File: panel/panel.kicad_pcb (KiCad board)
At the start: 2 copper layers, 40 x 40 mm, 256 parts

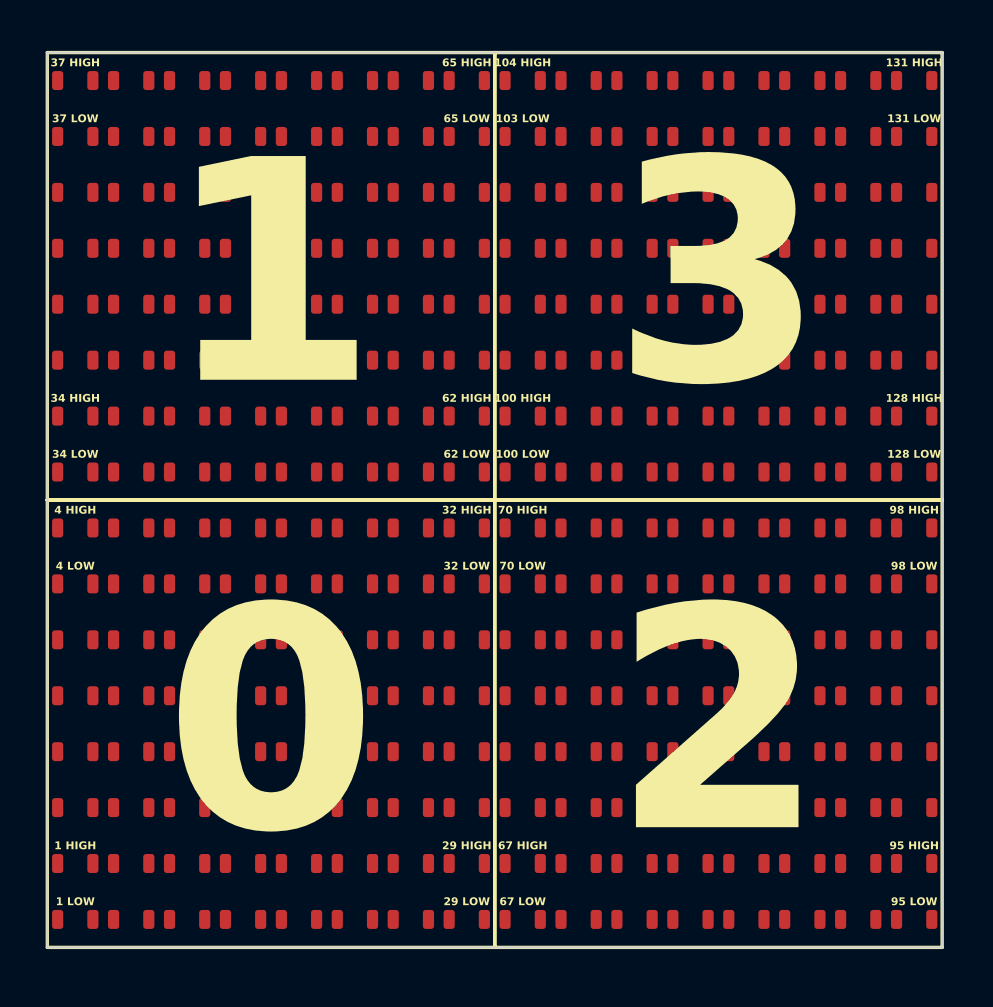
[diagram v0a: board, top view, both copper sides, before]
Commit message: Update pixel numbering
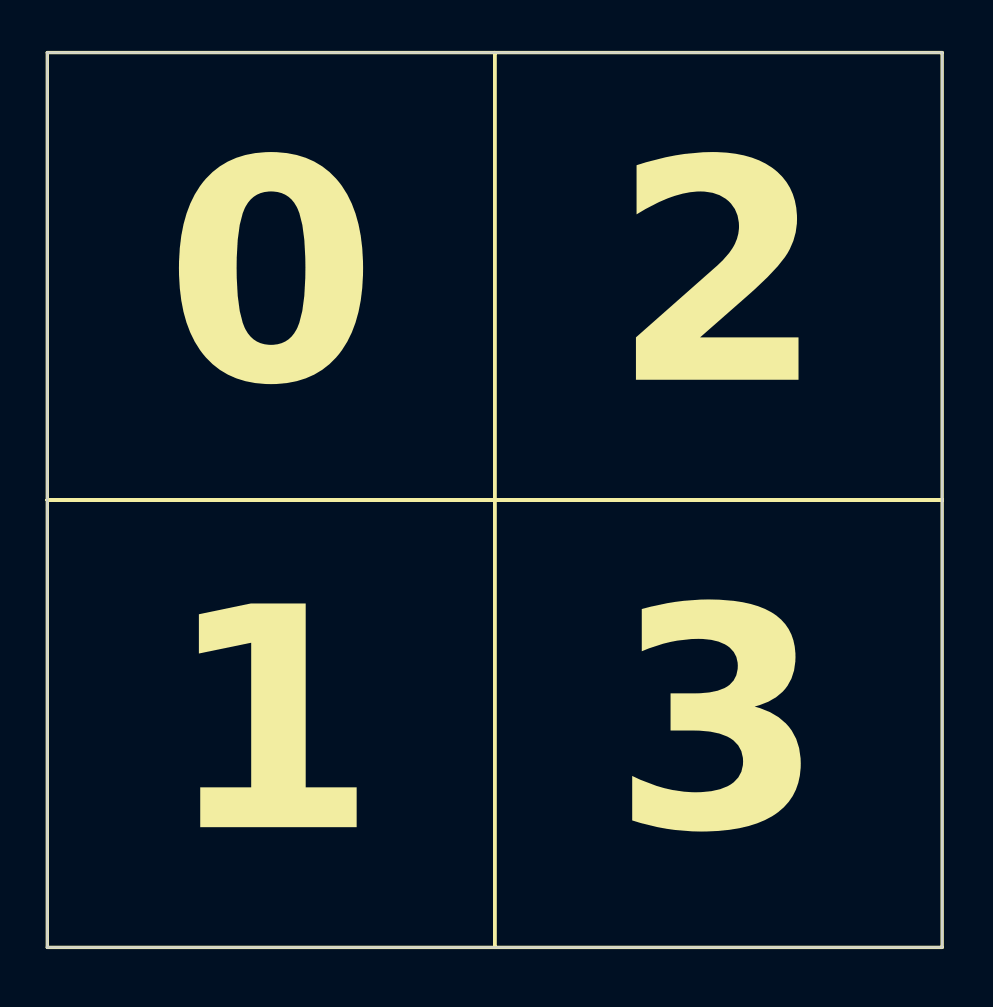
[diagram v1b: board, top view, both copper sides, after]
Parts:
- removed REF** (x256): LED_0603_1608Metric, LED_SMD:LED_0603_1608Metric

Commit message: Update panel
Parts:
- added REF**: LED_0402_1005Metric, LED_SMD:LED_0402_1005Metric, F.Cu at (146.2, 91.2)
- added REF**: LED_0402_1005Metric, LED_SMD:LED_0402_1005Metric, F.Cu at (138.8, 96.2)
- added REF**: LED_0402_1005Metric, LED_SMD:LED_0402_1005Metric, F.Cu at (116.2, 128.8)
- added REF**: LED_0402_1005Metric, LED_SMD:LED_0402_1005Metric, F.Cu at (116.2, 101.2)
- added REF**: LED_0402_1005Metric, LED_SMD:LED_0402_1005Metric, F.Cu at (153.8, 126.2)
- added REF**: LED_0402_1005Metric, LED_SMD:LED_0402_1005Metric, F.Cu at (151.2, 96.2)
- added REF**: LED_0402_1005Metric, LED_SMD:LED_0402_1005Metric, F.Cu at (118.8, 111.2)
- added REF**: LED_0402_1005Metric, LED_SMD:LED_0402_1005Metric, F.Cu at (128.8, 106.2)
- added REF**: LED_0402_1005Metric, LED_SMD:LED_0402_1005Metric, F.Cu at (131.2, 106.2)
- added REF**: LED_0402_1005Metric, LED_SMD:LED_0402_1005Metric, F.Cu at (116.2, 91.2)
- added REF**: LED_0402_1005Metric, LED_SMD:LED_0402_1005Metric, F.Cu at (128.8, 103.8)
- added REF**: LED_0402_1005Metric, LED_SMD:LED_0402_1005Metric, F.Cu at (138.8, 103.8)
- added REF**: LED_0402_1005Metric, LED_SMD:LED_0402_1005Metric, F.Cu at (126.2, 113.8)
- added REF**: LED_0402_1005Metric, LED_SMD:LED_0402_1005Metric, F.Cu at (121.2, 91.2)
- added REF**: LED_0402_1005Metric, LED_SMD:LED_0402_1005Metric, F.Cu at (138.8, 121.2)
- added REF**: LED_0402_1005Metric, LED_SMD:LED_0402_1005Metric, F.Cu at (136.2, 96.2)
- added REF**: LED_0402_1005Metric, LED_SMD:LED_0402_1005Metric, F.Cu at (153.8, 96.2)
- added REF**: LED_0402_1005Metric, LED_SMD:LED_0402_1005Metric, F.Cu at (153.8, 93.8)
- added REF**: LED_0402_1005Metric, LED_SMD:LED_0402_1005Metric, F.Cu at (148.8, 118.8)
- added REF**: LED_0402_1005Metric, LED_SMD:LED_0402_1005Metric, F.Cu at (138.8, 111.2)
- added REF**: LED_0402_1005Metric, LED_SMD:LED_0402_1005Metric, F.Cu at (118.8, 106.2)
- added REF**: LED_0402_1005Metric, LED_SMD:LED_0402_1005Metric, F.Cu at (116.2, 106.2)
- added REF**: LED_0402_1005Metric, LED_SMD:LED_0402_1005Metric, F.Cu at (131.2, 118.8)
- added REF**: LED_0402_1005Metric, LED_SMD:LED_0402_1005Metric, F.Cu at (136.2, 106.2)
- added REF**: LED_0402_1005Metric, LED_SMD:LED_0402_1005Metric, F.Cu at (128.8, 108.8)
- added REF**: LED_0402_1005Metric, LED_SMD:LED_0402_1005Metric, F.Cu at (143.8, 91.2)
- added REF**: LED_0402_1005Metric, LED_SMD:LED_0402_1005Metric, F.Cu at (128.8, 126.2)
- added REF**: LED_0402_1005Metric, LED_SMD:LED_0402_1005Metric, F.Cu at (126.2, 121.2)
- added REF**: LED_0402_1005Metric, LED_SMD:LED_0402_1005Metric, F.Cu at (131.2, 123.8)
- added REF**: LED_0402_1005Metric, LED_SMD:LED_0402_1005Metric, F.Cu at (148.8, 123.8)
- added REF**: LED_0402_1005Metric, LED_SMD:LED_0402_1005Metric, F.Cu at (131.2, 116.2)
- added REF**: LED_0402_1005Metric, LED_SMD:LED_0402_1005Metric, F.Cu at (141.2, 126.2)
- added REF**: LED_0402_1005Metric, LED_SMD:LED_0402_1005Metric, F.Cu at (128.8, 93.8)
- added REF**: LED_0402_1005Metric, LED_SMD:LED_0402_1005Metric, F.Cu at (136.2, 101.2)
- added REF**: LED_0402_1005Metric, LED_SMD:LED_0402_1005Metric, F.Cu at (131.2, 93.8)
- added REF**: LED_0402_1005Metric, LED_SMD:LED_0402_1005Metric, F.Cu at (128.8, 91.2)
- added REF**: LED_0402_1005Metric, LED_SMD:LED_0402_1005Metric, F.Cu at (118.8, 118.8)
- added REF**: LED_0402_1005Metric, LED_SMD:LED_0402_1005Metric, F.Cu at (128.8, 123.8)
- added REF**: LED_0402_1005Metric, LED_SMD:LED_0402_1005Metric, F.Cu at (136.2, 128.8)
- added REF**: LED_0402_1005Metric, LED_SMD:LED_0402_1005Metric, F.Cu at (116.2, 93.8)
- added REF**: LED_0402_1005Metric, LED_SMD:LED_0402_1005Metric, F.Cu at (133.8, 121.2)
- added REF**: LED_0402_1005Metric, LED_SMD:LED_0402_1005Metric, F.Cu at (123.8, 116.2)
- added REF**: LED_0402_1005Metric, LED_SMD:LED_0402_1005Metric, F.Cu at (118.8, 121.2)
- added REF**: LED_0402_1005Metric, LED_SMD:LED_0402_1005Metric, F.Cu at (126.2, 118.8)
- added REF**: LED_0402_1005Metric, LED_SMD:LED_0402_1005Metric, F.Cu at (148.8, 101.2)
- added REF**: LED_0402_1005Metric, LED_SMD:LED_0402_1005Metric, F.Cu at (118.8, 91.2)
- added REF**: LED_0402_1005Metric, LED_SMD:LED_0402_1005Metric, F.Cu at (141.2, 101.2)
- added REF**: LED_0402_1005Metric, LED_SMD:LED_0402_1005Metric, F.Cu at (143.8, 121.2)
- added REF**: LED_0402_1005Metric, LED_SMD:LED_0402_1005Metric, F.Cu at (128.8, 101.2)
- added REF**: LED_0402_1005Metric, LED_SMD:LED_0402_1005Metric, F.Cu at (143.8, 111.2)
- added REF**: LED_0402_1005Metric, LED_SMD:LED_0402_1005Metric, F.Cu at (148.8, 108.8)
- added REF**: LED_0402_1005Metric, LED_SMD:LED_0402_1005Metric, F.Cu at (121.2, 116.2)
- added REF**: LED_0402_1005Metric, LED_SMD:LED_0402_1005Metric, F.Cu at (153.8, 121.2)
- added REF**: LED_0402_1005Metric, LED_SMD:LED_0402_1005Metric, F.Cu at (126.2, 93.8)
- added REF**: LED_0402_1005Metric, LED_SMD:LED_0402_1005Metric, F.Cu at (118.8, 93.8)
- added REF**: LED_0402_1005Metric, LED_SMD:LED_0402_1005Metric, F.Cu at (143.8, 128.8)
- added REF**: LED_0402_1005Metric, LED_SMD:LED_0402_1005Metric, F.Cu at (133.8, 108.8)
- added REF**: LED_0402_1005Metric, LED_SMD:LED_0402_1005Metric, F.Cu at (138.8, 123.8)
- added REF**: LED_0402_1005Metric, LED_SMD:LED_0402_1005Metric, F.Cu at (123.8, 103.8)
- added REF**: LED_0402_1005Metric, LED_SMD:LED_0402_1005Metric, F.Cu at (138.8, 128.8)
- added REF**: LED_0402_1005Metric, LED_SMD:LED_0402_1005Metric, F.Cu at (131.2, 98.8)
- added REF**: LED_0402_1005Metric, LED_SMD:LED_0402_1005Metric, F.Cu at (126.2, 111.2)
- added REF**: LED_0402_1005Metric, LED_SMD:LED_0402_1005Metric, F.Cu at (153.8, 111.2)
- added REF**: LED_0402_1005Metric, LED_SMD:LED_0402_1005Metric, F.Cu at (153.8, 113.8)
- added REF**: LED_0402_1005Metric, LED_SMD:LED_0402_1005Metric, F.Cu at (148.8, 126.2)
- added REF**: LED_0402_1005Metric, LED_SMD:LED_0402_1005Metric, F.Cu at (133.8, 103.8)
- added REF**: LED_0402_1005Metric, LED_SMD:LED_0402_1005Metric, F.Cu at (133.8, 96.2)
- added REF**: LED_0402_1005Metric, LED_SMD:LED_0402_1005Metric, F.Cu at (131.2, 108.8)
- added REF**: LED_0402_1005Metric, LED_SMD:LED_0402_1005Metric, F.Cu at (136.2, 111.2)
- added REF**: LED_0402_1005Metric, LED_SMD:LED_0402_1005Metric, F.Cu at (121.2, 113.8)
- added REF**: LED_0402_1005Metric, LED_SMD:LED_0402_1005Metric, F.Cu at (141.2, 106.2)
- added REF**: LED_0402_1005Metric, LED_SMD:LED_0402_1005Metric, F.Cu at (128.8, 128.8)
- added REF**: LED_0402_1005Metric, LED_SMD:LED_0402_1005Metric, F.Cu at (146.2, 103.8)
- added REF**: LED_0402_1005Metric, LED_SMD:LED_0402_1005Metric, F.Cu at (141.2, 121.2)
- added REF**: LED_0402_1005Metric, LED_SMD:LED_0402_1005Metric, F.Cu at (146.2, 106.2)
- added REF**: LED_0402_1005Metric, LED_SMD:LED_0402_1005Metric, F.Cu at (153.8, 123.8)
- added REF**: LED_0402_1005Metric, LED_SMD:LED_0402_1005Metric, F.Cu at (118.8, 113.8)
- added REF**: LED_0402_1005Metric, LED_SMD:LED_0402_1005Metric, F.Cu at (153.8, 98.8)
- added REF**: LED_0402_1005Metric, LED_SMD:LED_0402_1005Metric, F.Cu at (143.8, 98.8)
- added REF**: LED_0402_1005Metric, LED_SMD:LED_0402_1005Metric, F.Cu at (116.2, 96.2)
- added REF**: LED_0402_1005Metric, LED_SMD:LED_0402_1005Metric, F.Cu at (138.8, 98.8)
- added REF**: LED_0402_1005Metric, LED_SMD:LED_0402_1005Metric, F.Cu at (118.8, 116.2)
- added REF**: LED_0402_1005Metric, LED_SMD:LED_0402_1005Metric, F.Cu at (143.8, 103.8)
- added REF**: LED_0402_1005Metric, LED_SMD:LED_0402_1005Metric, F.Cu at (126.2, 128.8)
- added REF**: LED_0402_1005Metric, LED_SMD:LED_0402_1005Metric, F.Cu at (138.8, 113.8)
- added REF**: LED_0402_1005Metric, LED_SMD:LED_0402_1005Metric, F.Cu at (133.8, 113.8)
- added REF**: LED_0402_1005Metric, LED_SMD:LED_0402_1005Metric, F.Cu at (118.8, 101.2)
- added REF**: LED_0402_1005Metric, LED_SMD:LED_0402_1005Metric, F.Cu at (138.8, 93.8)
- added REF**: LED_0402_1005Metric, LED_SMD:LED_0402_1005Metric, F.Cu at (131.2, 113.8)
- added REF**: LED_0402_1005Metric, LED_SMD:LED_0402_1005Metric, F.Cu at (116.2, 111.2)
- added REF**: LED_0402_1005Metric, LED_SMD:LED_0402_1005Metric, F.Cu at (126.2, 96.2)
- added REF**: LED_0402_1005Metric, LED_SMD:LED_0402_1005Metric, F.Cu at (118.8, 108.8)
- added REF**: LED_0402_1005Metric, LED_SMD:LED_0402_1005Metric, F.Cu at (126.2, 116.2)
- added REF**: LED_0402_1005Metric, LED_SMD:LED_0402_1005Metric, F.Cu at (143.8, 106.2)
- added REF**: LED_0402_1005Metric, LED_SMD:LED_0402_1005Metric, F.Cu at (116.2, 108.8)
- added REF**: LED_0402_1005Metric, LED_SMD:LED_0402_1005Metric, F.Cu at (136.2, 121.2)
- added REF**: LED_0402_1005Metric, LED_SMD:LED_0402_1005Metric, F.Cu at (121.2, 103.8)
- added REF**: LED_0402_1005Metric, LED_SMD:LED_0402_1005Metric, F.Cu at (138.8, 108.8)
- added REF**: LED_0402_1005Metric, LED_SMD:LED_0402_1005Metric, F.Cu at (133.8, 93.8)
- added REF**: LED_0402_1005Metric, LED_SMD:LED_0402_1005Metric, F.Cu at (148.8, 93.8)
- added REF**: LED_0402_1005Metric, LED_SMD:LED_0402_1005Metric, F.Cu at (116.2, 126.2)
- added REF**: LED_0402_1005Metric, LED_SMD:LED_0402_1005Metric, F.Cu at (146.2, 101.2)
- added REF**: LED_0402_1005Metric, LED_SMD:LED_0402_1005Metric, F.Cu at (123.8, 123.8)
- added REF**: LED_0402_1005Metric, LED_SMD:LED_0402_1005Metric, F.Cu at (121.2, 126.2)
- added REF**: LED_0402_1005Metric, LED_SMD:LED_0402_1005Metric, F.Cu at (148.8, 116.2)
- added REF**: LED_0402_1005Metric, LED_SMD:LED_0402_1005Metric, F.Cu at (116.2, 123.8)
- added REF**: LED_0402_1005Metric, LED_SMD:LED_0402_1005Metric, F.Cu at (131.2, 126.2)
- added REF**: LED_0402_1005Metric, LED_SMD:LED_0402_1005Metric, F.Cu at (131.2, 96.2)
- added REF**: LED_0402_1005Metric, LED_SMD:LED_0402_1005Metric, F.Cu at (118.8, 123.8)
- added REF**: LED_0402_1005Metric, LED_SMD:LED_0402_1005Metric, F.Cu at (138.8, 106.2)
- added REF**: LED_0402_1005Metric, LED_SMD:LED_0402_1005Metric, F.Cu at (141.2, 96.2)
- added REF**: LED_0402_1005Metric, LED_SMD:LED_0402_1005Metric, F.Cu at (153.8, 116.2)
- added REF**: LED_0402_1005Metric, LED_SMD:LED_0402_1005Metric, F.Cu at (118.8, 126.2)
- added REF**: LED_0402_1005Metric, LED_SMD:LED_0402_1005Metric, F.Cu at (151.2, 123.8)
- added REF**: LED_0402_1005Metric, LED_SMD:LED_0402_1005Metric, F.Cu at (133.8, 128.8)
- added REF**: LED_0402_1005Metric, LED_SMD:LED_0402_1005Metric, F.Cu at (143.8, 116.2)
- added REF**: LED_0402_1005Metric, LED_SMD:LED_0402_1005Metric, F.Cu at (128.8, 98.8)
- added REF**: LED_0402_1005Metric, LED_SMD:LED_0402_1005Metric, F.Cu at (141.2, 118.8)
- added REF**: LED_0402_1005Metric, LED_SMD:LED_0402_1005Metric, F.Cu at (148.8, 121.2)
- added REF**: LED_0402_1005Metric, LED_SMD:LED_0402_1005Metric, F.Cu at (141.2, 116.2)
- added REF**: LED_0402_1005Metric, LED_SMD:LED_0402_1005Metric, F.Cu at (141.2, 98.8)
- added REF**: LED_0402_1005Metric, LED_SMD:LED_0402_1005Metric, F.Cu at (136.2, 126.2)
- added REF**: LED_0402_1005Metric, LED_SMD:LED_0402_1005Metric, F.Cu at (136.2, 108.8)
- added REF**: LED_0402_1005Metric, LED_SMD:LED_0402_1005Metric, F.Cu at (116.2, 121.2)
- added REF**: LED_0402_1005Metric, LED_SMD:LED_0402_1005Metric, F.Cu at (141.2, 111.2)
- added REF**: LED_0402_1005Metric, LED_SMD:LED_0402_1005Metric, F.Cu at (126.2, 103.8)
- added REF**: LED_0402_1005Metric, LED_SMD:LED_0402_1005Metric, F.Cu at (146.2, 108.8)
- added REF**: LED_0402_1005Metric, LED_SMD:LED_0402_1005Metric, F.Cu at (143.8, 113.8)
- added REF**: LED_0402_1005Metric, LED_SMD:LED_0402_1005Metric, F.Cu at (146.2, 126.2)
- added REF**: LED_0402_1005Metric, LED_SMD:LED_0402_1005Metric, F.Cu at (121.2, 108.8)
- added REF**: LED_0402_1005Metric, LED_SMD:LED_0402_1005Metric, F.Cu at (126.2, 123.8)
- added REF**: LED_0402_1005Metric, LED_SMD:LED_0402_1005Metric, F.Cu at (123.8, 106.2)
- added REF**: LED_0402_1005Metric, LED_SMD:LED_0402_1005Metric, F.Cu at (121.2, 118.8)
- added REF**: LED_0402_1005Metric, LED_SMD:LED_0402_1005Metric, F.Cu at (131.2, 101.2)
- added REF**: LED_0402_1005Metric, LED_SMD:LED_0402_1005Metric, F.Cu at (131.2, 111.2)
- added REF**: LED_0402_1005Metric, LED_SMD:LED_0402_1005Metric, F.Cu at (126.2, 106.2)
- added REF**: LED_0402_1005Metric, LED_SMD:LED_0402_1005Metric, F.Cu at (128.8, 96.2)
- added REF**: LED_0402_1005Metric, LED_SMD:LED_0402_1005Metric, F.Cu at (136.2, 103.8)
- added REF**: LED_0402_1005Metric, LED_SMD:LED_0402_1005Metric, F.Cu at (126.2, 108.8)
- added REF**: LED_0402_1005Metric, LED_SMD:LED_0402_1005Metric, F.Cu at (153.8, 106.2)
- added REF**: LED_0402_1005Metric, LED_SMD:LED_0402_1005Metric, F.Cu at (143.8, 93.8)
- added REF**: LED_0402_1005Metric, LED_SMD:LED_0402_1005Metric, F.Cu at (118.8, 96.2)
- added REF**: LED_0402_1005Metric, LED_SMD:LED_0402_1005Metric, F.Cu at (151.2, 113.8)
- added REF**: LED_0402_1005Metric, LED_SMD:LED_0402_1005Metric, F.Cu at (146.2, 123.8)
- added REF**: LED_0402_1005Metric, LED_SMD:LED_0402_1005Metric, F.Cu at (151.2, 101.2)
- added REF**: LED_0402_1005Metric, LED_SMD:LED_0402_1005Metric, F.Cu at (141.2, 123.8)
- added REF**: LED_0402_1005Metric, LED_SMD:LED_0402_1005Metric, F.Cu at (128.8, 116.2)
- added REF**: LED_0402_1005Metric, LED_SMD:LED_0402_1005Metric, F.Cu at (153.8, 128.8)
- added REF**: LED_0402_1005Metric, LED_SMD:LED_0402_1005Metric, F.Cu at (151.2, 108.8)
- added REF**: LED_0402_1005Metric, LED_SMD:LED_0402_1005Metric, F.Cu at (133.8, 91.2)
- added REF**: LED_0402_1005Metric, LED_SMD:LED_0402_1005Metric, F.Cu at (148.8, 111.2)
- added REF**: LED_0402_1005Metric, LED_SMD:LED_0402_1005Metric, F.Cu at (148.8, 128.8)
- added REF**: LED_0402_1005Metric, LED_SMD:LED_0402_1005Metric, F.Cu at (153.8, 91.2)
- added REF**: LED_0402_1005Metric, LED_SMD:LED_0402_1005Metric, F.Cu at (148.8, 106.2)
- added REF**: LED_0402_1005Metric, LED_SMD:LED_0402_1005Metric, F.Cu at (143.8, 123.8)
- added REF**: LED_0402_1005Metric, LED_SMD:LED_0402_1005Metric, F.Cu at (141.2, 113.8)
- added REF**: LED_0402_1005Metric, LED_SMD:LED_0402_1005Metric, F.Cu at (126.2, 98.8)
- added REF**: LED_0402_1005Metric, LED_SMD:LED_0402_1005Metric, F.Cu at (131.2, 103.8)
- added REF**: LED_0402_1005Metric, LED_SMD:LED_0402_1005Metric, F.Cu at (116.2, 103.8)
- added REF**: LED_0402_1005Metric, LED_SMD:LED_0402_1005Metric, F.Cu at (123.8, 91.2)
- added REF**: LED_0402_1005Metric, LED_SMD:LED_0402_1005Metric, F.Cu at (116.2, 116.2)
- added REF**: LED_0402_1005Metric, LED_SMD:LED_0402_1005Metric, F.Cu at (138.8, 126.2)
- added REF**: LED_0402_1005Metric, LED_SMD:LED_0402_1005Metric, F.Cu at (146.2, 98.8)
- added REF**: LED_0402_1005Metric, LED_SMD:LED_0402_1005Metric, F.Cu at (136.2, 118.8)
- added REF**: LED_0402_1005Metric, LED_SMD:LED_0402_1005Metric, F.Cu at (148.8, 113.8)
- added REF**: LED_0402_1005Metric, LED_SMD:LED_0402_1005Metric, F.Cu at (151.2, 128.8)
- added REF**: LED_0402_1005Metric, LED_SMD:LED_0402_1005Metric, F.Cu at (136.2, 98.8)
- added REF**: LED_0402_1005Metric, LED_SMD:LED_0402_1005Metric, F.Cu at (123.8, 101.2)
- added REF**: LED_0402_1005Metric, LED_SMD:LED_0402_1005Metric, F.Cu at (136.2, 116.2)
- added REF**: LED_0402_1005Metric, LED_SMD:LED_0402_1005Metric, F.Cu at (153.8, 108.8)
- added REF**: LED_0402_1005Metric, LED_SMD:LED_0402_1005Metric, F.Cu at (146.2, 116.2)
- added REF**: LED_0402_1005Metric, LED_SMD:LED_0402_1005Metric, F.Cu at (138.8, 101.2)
- added REF**: LED_0402_1005Metric, LED_SMD:LED_0402_1005Metric, F.Cu at (153.8, 118.8)
- added REF**: LED_0402_1005Metric, LED_SMD:LED_0402_1005Metric, F.Cu at (123.8, 111.2)
- added REF**: LED_0402_1005Metric, LED_SMD:LED_0402_1005Metric, F.Cu at (146.2, 93.8)
- added REF**: LED_0402_1005Metric, LED_SMD:LED_0402_1005Metric, F.Cu at (136.2, 91.2)
- added REF**: LED_0402_1005Metric, LED_SMD:LED_0402_1005Metric, F.Cu at (118.8, 98.8)
- added REF**: LED_0402_1005Metric, LED_SMD:LED_0402_1005Metric, F.Cu at (123.8, 96.2)
- added REF**: LED_0402_1005Metric, LED_SMD:LED_0402_1005Metric, F.Cu at (148.8, 91.2)
- added REF**: LED_0402_1005Metric, LED_SMD:LED_0402_1005Metric, F.Cu at (143.8, 96.2)
- added REF**: LED_0402_1005Metric, LED_SMD:LED_0402_1005Metric, F.Cu at (133.8, 111.2)
- added REF**: LED_0402_1005Metric, LED_SMD:LED_0402_1005Metric, F.Cu at (146.2, 113.8)
- added REF**: LED_0402_1005Metric, LED_SMD:LED_0402_1005Metric, F.Cu at (151.2, 91.2)
- added REF**: LED_0402_1005Metric, LED_SMD:LED_0402_1005Metric, F.Cu at (143.8, 101.2)
- added REF**: LED_0402_1005Metric, LED_SMD:LED_0402_1005Metric, F.Cu at (133.8, 106.2)
- added REF**: LED_0402_1005Metric, LED_SMD:LED_0402_1005Metric, F.Cu at (123.8, 121.2)
- added REF**: LED_0402_1005Metric, LED_SMD:LED_0402_1005Metric, F.Cu at (121.2, 93.8)
- added REF**: LED_0402_1005Metric, LED_SMD:LED_0402_1005Metric, F.Cu at (128.8, 111.2)
- added REF**: LED_0402_1005Metric, LED_SMD:LED_0402_1005Metric, F.Cu at (151.2, 118.8)
- added REF**: LED_0402_1005Metric, LED_SMD:LED_0402_1005Metric, F.Cu at (143.8, 118.8)
- added REF**: LED_0402_1005Metric, LED_SMD:LED_0402_1005Metric, F.Cu at (136.2, 113.8)
- added REF**: LED_0402_1005Metric, LED_SMD:LED_0402_1005Metric, F.Cu at (123.8, 113.8)
- added REF**: LED_0402_1005Metric, LED_SMD:LED_0402_1005Metric, F.Cu at (121.2, 123.8)
- added REF**: LED_0402_1005Metric, LED_SMD:LED_0402_1005Metric, F.Cu at (126.2, 91.2)
- added REF**: LED_0402_1005Metric, LED_SMD:LED_0402_1005Metric, F.Cu at (138.8, 91.2)
- added REF**: LED_0402_1005Metric, LED_SMD:LED_0402_1005Metric, F.Cu at (151.2, 98.8)
- added REF**: LED_0402_1005Metric, LED_SMD:LED_0402_1005Metric, F.Cu at (133.8, 118.8)
- added REF**: LED_0402_1005Metric, LED_SMD:LED_0402_1005Metric, F.Cu at (116.2, 118.8)
- added REF**: LED_0402_1005Metric, LED_SMD:LED_0402_1005Metric, F.Cu at (136.2, 93.8)
- added REF**: LED_0402_1005Metric, LED_SMD:LED_0402_1005Metric, F.Cu at (138.8, 118.8)
- added REF**: LED_0402_1005Metric, LED_SMD:LED_0402_1005Metric, F.Cu at (123.8, 128.8)
- added REF**: LED_0402_1005Metric, LED_SMD:LED_0402_1005Metric, F.Cu at (123.8, 98.8)
- added REF**: LED_0402_1005Metric, LED_SMD:LED_0402_1005Metric, F.Cu at (123.8, 126.2)
- added REF**: LED_0402_1005Metric, LED_SMD:LED_0402_1005Metric, F.Cu at (131.2, 121.2)
- added REF**: LED_0402_1005Metric, LED_SMD:LED_0402_1005Metric, F.Cu at (133.8, 116.2)
- added REF**: LED_0402_1005Metric, LED_SMD:LED_0402_1005Metric, F.Cu at (121.2, 121.2)
- added REF**: LED_0402_1005Metric, LED_SMD:LED_0402_1005Metric, F.Cu at (133.8, 101.2)
- added REF**: LED_0402_1005Metric, LED_SMD:LED_0402_1005Metric, F.Cu at (133.8, 126.2)
- added REF**: LED_0402_1005Metric, LED_SMD:LED_0402_1005Metric, F.Cu at (116.2, 98.8)
- added REF**: LED_0402_1005Metric, LED_SMD:LED_0402_1005Metric, F.Cu at (141.2, 93.8)
- added REF**: LED_0402_1005Metric, LED_SMD:LED_0402_1005Metric, F.Cu at (141.2, 103.8)
- added REF**: LED_0402_1005Metric, LED_SMD:LED_0402_1005Metric, F.Cu at (133.8, 123.8)
- added REF**: LED_0402_1005Metric, LED_SMD:LED_0402_1005Metric, F.Cu at (148.8, 98.8)
- added REF**: LED_0402_1005Metric, LED_SMD:LED_0402_1005Metric, F.Cu at (118.8, 103.8)
- added REF**: LED_0402_1005Metric, LED_SMD:LED_0402_1005Metric, F.Cu at (121.2, 128.8)
- added REF**: LED_0402_1005Metric, LED_SMD:LED_0402_1005Metric, F.Cu at (121.2, 111.2)
- added REF**: LED_0402_1005Metric, LED_SMD:LED_0402_1005Metric, F.Cu at (143.8, 108.8)
- added REF**: LED_0402_1005Metric, LED_SMD:LED_0402_1005Metric, F.Cu at (128.8, 118.8)
- added REF**: LED_0402_1005Metric, LED_SMD:LED_0402_1005Metric, F.Cu at (131.2, 128.8)
- added REF**: LED_0402_1005Metric, LED_SMD:LED_0402_1005Metric, F.Cu at (136.2, 123.8)
- added REF**: LED_0402_1005Metric, LED_SMD:LED_0402_1005Metric, F.Cu at (146.2, 96.2)
- added REF**: LED_0402_1005Metric, LED_SMD:LED_0402_1005Metric, F.Cu at (118.8, 128.8)
- added REF**: LED_0402_1005Metric, LED_SMD:LED_0402_1005Metric, F.Cu at (133.8, 98.8)
- added REF**: LED_0402_1005Metric, LED_SMD:LED_0402_1005Metric, F.Cu at (151.2, 103.8)
- added REF**: LED_0402_1005Metric, LED_SMD:LED_0402_1005Metric, F.Cu at (121.2, 96.2)
- added REF**: LED_0402_1005Metric, LED_SMD:LED_0402_1005Metric, F.Cu at (141.2, 128.8)
- added REF**: LED_0402_1005Metric, LED_SMD:LED_0402_1005Metric, F.Cu at (138.8, 116.2)
- added REF**: LED_0402_1005Metric, LED_SMD:LED_0402_1005Metric, F.Cu at (146.2, 128.8)
- added REF**: LED_0402_1005Metric, LED_SMD:LED_0402_1005Metric, F.Cu at (151.2, 93.8)
- added REF**: LED_0402_1005Metric, LED_SMD:LED_0402_1005Metric, F.Cu at (123.8, 118.8)
- added REF**: LED_0402_1005Metric, LED_SMD:LED_0402_1005Metric, F.Cu at (141.2, 108.8)
- added REF**: LED_0402_1005Metric, LED_SMD:LED_0402_1005Metric, F.Cu at (121.2, 101.2)
- added REF**: LED_0402_1005Metric, LED_SMD:LED_0402_1005Metric, F.Cu at (121.2, 98.8)
- added REF**: LED_0402_1005Metric, LED_SMD:LED_0402_1005Metric, F.Cu at (153.8, 101.2)
- added REF**: LED_0402_1005Metric, LED_SMD:LED_0402_1005Metric, F.Cu at (128.8, 113.8)
- added REF**: LED_0402_1005Metric, LED_SMD:LED_0402_1005Metric, F.Cu at (151.2, 111.2)
- added REF**: LED_0402_1005Metric, LED_SMD:LED_0402_1005Metric, F.Cu at (128.8, 121.2)
- added REF**: LED_0402_1005Metric, LED_SMD:LED_0402_1005Metric, F.Cu at (151.2, 126.2)
- added REF**: LED_0402_1005Metric, LED_SMD:LED_0402_1005Metric, F.Cu at (126.2, 101.2)
- added REF**: LED_0402_1005Metric, LED_SMD:LED_0402_1005Metric, F.Cu at (131.2, 91.2)
- added REF**: LED_0402_1005Metric, LED_SMD:LED_0402_1005Metric, F.Cu at (146.2, 111.2)
- added REF**: LED_0402_1005Metric, LED_SMD:LED_0402_1005Metric, F.Cu at (141.2, 91.2)
- added REF**: LED_0402_1005Metric, LED_SMD:LED_0402_1005Metric, F.Cu at (146.2, 121.2)
- added REF**: LED_0402_1005Metric, LED_SMD:LED_0402_1005Metric, F.Cu at (143.8, 126.2)
- added REF**: LED_0402_1005Metric, LED_SMD:LED_0402_1005Metric, F.Cu at (151.2, 106.2)
- added REF**: LED_0402_1005Metric, LED_SMD:LED_0402_1005Metric, F.Cu at (123.8, 108.8)
- added REF**: LED_0402_1005Metric, LED_SMD:LED_0402_1005Metric, F.Cu at (148.8, 96.2)
- added REF**: LED_0402_1005Metric, LED_SMD:LED_0402_1005Metric, F.Cu at (151.2, 121.2)
- added REF**: LED_0402_1005Metric, LED_SMD:LED_0402_1005Metric, F.Cu at (116.2, 113.8)
- added REF**: LED_0402_1005Metric, LED_SMD:LED_0402_1005Metric, F.Cu at (123.8, 93.8)
- added REF**: LED_0402_1005Metric, LED_SMD:LED_0402_1005Metric, F.Cu at (146.2, 118.8)
- added REF**: LED_0402_1005Metric, LED_SMD:LED_0402_1005Metric, F.Cu at (126.2, 126.2)
- added REF**: LED_0402_1005Metric, LED_SMD:LED_0402_1005Metric, F.Cu at (153.8, 103.8)
- added REF**: LED_0402_1005Metric, LED_SMD:LED_0402_1005Metric, F.Cu at (151.2, 116.2)
- added REF**: LED_0402_1005Metric, LED_SMD:LED_0402_1005Metric, F.Cu at (148.8, 103.8)
- added REF**: LED_0402_1005Metric, LED_SMD:LED_0402_1005Metric, F.Cu at (121.2, 106.2)
